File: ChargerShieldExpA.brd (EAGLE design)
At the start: 160 x 99.1 mm, 101 parts, among them IC1 TL431, IC2 LM324N, Q1 BUZ11, Q2 BD648, Q3 BUZ171, Q4 IRFZ48Z, T1 BC548, X1 +Vin, X2 VCC, X3 Battery

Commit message: update
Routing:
- net GND: track 168.7 -> 169.3 mm
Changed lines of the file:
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@@
 <setting verticaltext="up"/>
 </settings>
-<grid distance="1.27" unitdist="mm" unit="mm" style="lines" multiple="2" display="yes" altdistance="0.15875" altunitdist="mm" altunit="mm"/>
+<grid distance="0.05" unitdist="inch" unit="mm" style="lines" multiple="1" display="yes" altdistance="0.025" altunitdist="inch" altunit="mm"/>
 <layers>
 <layer number="1" name="Top" color="4" fill="1" visible="yes" active="yes"/>
@@
 <wire x1="19.05" y1="11.43" x2="19.05" y2="-3.81" width="0.8128" layer="1" style="shortdash"/>
 <contactref element="JP20" pad="3"/>
-<via x="5.08" y="38.1" extent="1-16" drill="0.8" shape="square"/>
+<via x="5.08" y="38.1" extent="1-16" drill="1" shape="square"/>
 <wire x1="22.86" y1="-7.62" x2="22.86" y2="-11.47" width="1.6764" layer="16"/>
 <wire x1="22.86" y1="-11.47" x2="22.82" y2="-10.16" width="1.6764" layer="16"/>
@@
 <contactref element="S4" pad="1"/>
 <contactref element="S5" pad="1"/>
-<via x="1.27" y="38.1" extent="1-16" drill="0.8" shape="square"/>
-<wire x1="1.27" y1="38.1" x2="5.08" y2="38.1" width="0.8128" layer="1"/>
+<via x="0.635" y="38.1" extent="1-16" drill="1" shape="square"/>
+<wire x1="0.635" y1="38.1" x2="5.08" y2="38.1" width="0.8128" layer="1"/>
 <wire x1="2.54" y1="33.02" x2="2.54" y2="12.7" width="2.54" layer="16"/>
 <wire x1="2.54" y1="33.02" x2="6.35" y2="33.02" width="2.54" layer="16"/>
@@
 <polygon width="1.27" layer="16" isolate="0.6096" orphans="yes">
 <vertex x="0" y="-15.24"/>
-<vertex x="1.27" y="53.34"/>
+<vertex x="0" y="35.56"/>
+<vertex x="-12.7" y="35.56"/>
+<vertex x="-12.7" y="53.34"/>
 <vertex x="-41.91" y="53.34"/>
 <vertex x="-43.18" y="-15.24"/>
@@
 <wire x1="-27.94" y1="59.69" x2="-27.94" y2="58.42" width="0.8128" layer="16"/>
 <wire x1="-27.94" y1="58.42" x2="-11.43" y2="41.91" width="0.8128" layer="16"/>
-<wire x1="-11.43" y1="41.91" x2="-11.43" y2="29.21" width="0.8128" layer="16"/>
+<wire x1="-11.43" y1="41.91" x2="-11.43" y2="27.94" width="0.8128" layer="16"/>
 <wire x1="-40.64" y1="17.78" x2="-40.64" y2="8.1788" width="0.8128" layer="16"/>
 <wire x1="-40.64" y1="8.1788" x2="-38.735" y2="6.2738" width="0.8128" layer="16"/>
-<wire x1="-11.43" y1="29.21" x2="-16.51" y2="24.13" width="0.8128" layer="16"/>
-<wire x1="-16.51" y1="24.13" x2="-16.51" y2="17.78" width="0.8128" layer="16"/>
+<wire x1="-11.43" y1="27.94" x2="-16.51" y2="22.86" width="0.8128" layer="16"/>
+<wire x1="-16.51" y1="22.86" x2="-16.51" y2="17.78" width="0.8128" layer="16"/>
 <wire x1="-16.51" y1="17.78" x2="-40.64" y2="17.78" width="0.8128" layer="16"/>
 <contactref element="U$3" pad="6"/>

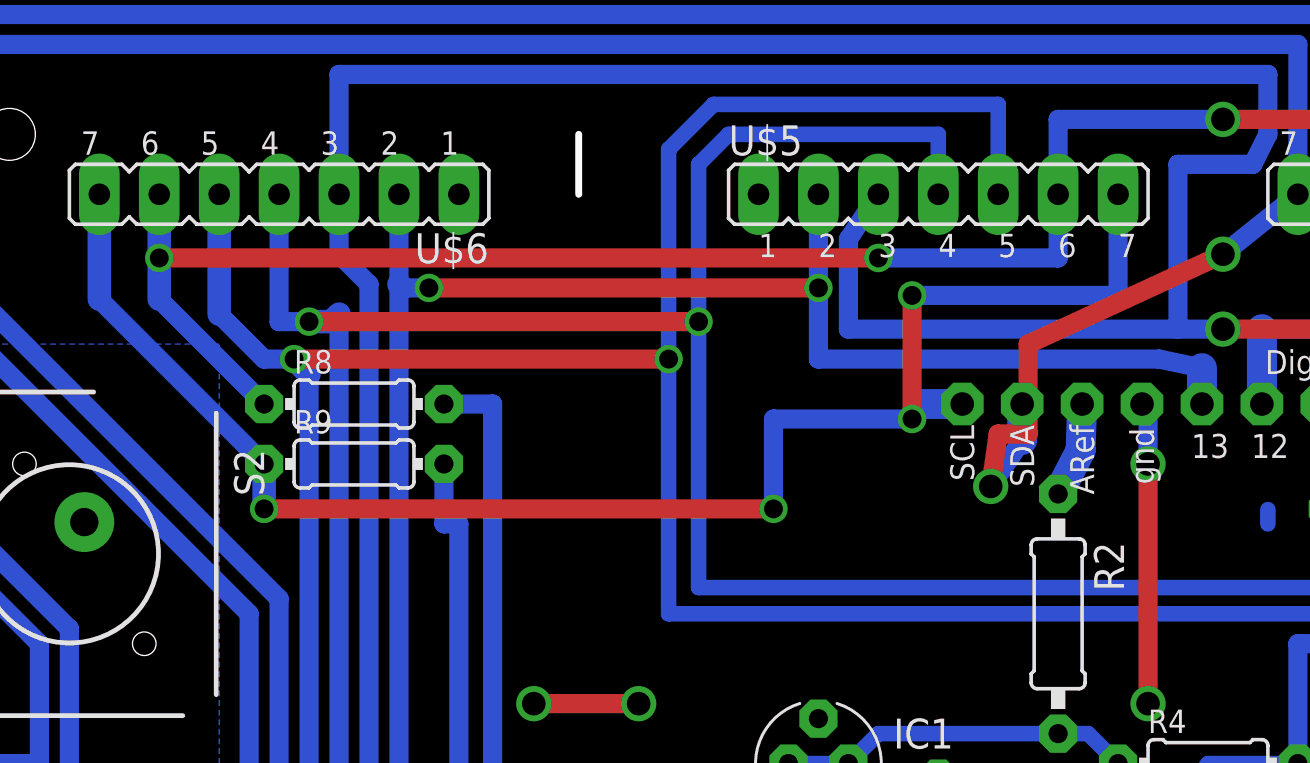
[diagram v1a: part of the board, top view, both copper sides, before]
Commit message: via drills should be 1mm
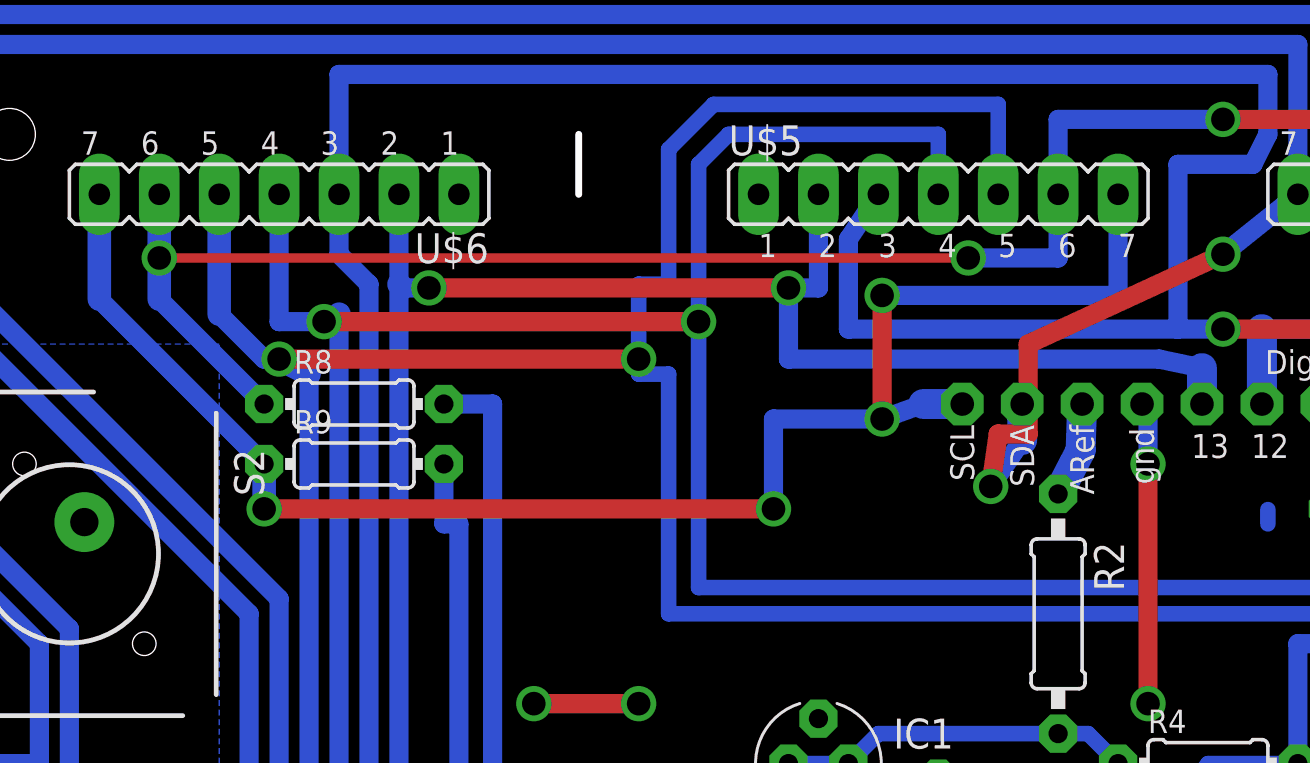
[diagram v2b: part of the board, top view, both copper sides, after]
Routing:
- net PWM_DISCHARGE2: track 188.2 -> 190.0 mm
- net N$1: track 101.7 -> 103.0 mm
- net N$41: track 68.2 -> 69.3 mm
- net PWM_DISCHARGE1: track 170.6 -> 170.0 mm
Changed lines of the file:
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@@
 <wire x1="28.956" y1="50.8" x2="28.956" y2="52.324" width="1.27" layer="16"/>
 <wire x1="28.956" y1="52.324" x2="27.14625" y2="52.705" width="0.8128" layer="16"/>
-<wire x1="27.14625" y1="52.705" x2="12.7" y2="52.705" width="0.8128" layer="16"/>
-<wire x1="12.7" y1="52.705" x2="12.7" y2="55.72125" width="0.8128" layer="16"/>
+<wire x1="27.14625" y1="52.705" x2="11.43" y2="52.705" width="0.8128" layer="16"/>
+<wire x1="11.43" y1="52.705" x2="11.43" y2="55.72125" width="0.8128" layer="16"/>
 <contactref element="R3" pad="2"/>
 <contactref element="U$6" pad="2"/>
+<wire x1="11.43" y1="55.72125" x2="12.7" y2="55.72125" width="0.8128" layer="16"/>
 <wire x1="12.7" y1="55.72125" x2="12.7" y2="59.69" width="0.8128" layer="16"/>
 <wire x1="-4.445" y1="1.27" x2="-4.445" y2="2.54" width="0.8128" layer="16"/>
@@
 <wire x1="-3.81" y1="55.72125" x2="-4.92125" y2="55.72125" width="0.8128" layer="16"/>
 <wire x1="-5.08" y1="55.88" x2="-5.08" y2="59.69" width="0.8128" layer="16"/>
-<wire x1="-3.81" y1="55.72125" x2="12.7" y2="55.72125" width="0.8128" layer="1"/>
-<via x="12.7" y="55.72125" extent="1-16" drill="0.8" shape="square"/>
-<via x="-3.81" y="55.72125" extent="1-16" drill="0.8" shape="square"/>
+<wire x1="-3.81" y1="55.72125" x2="11.43" y2="55.72125" width="0.8128" layer="1"/>
+<via x="11.43" y="55.72125" extent="1-16" drill="1" shape="square"/>
+<via x="-3.81" y="55.72125" extent="1-16" drill="1" shape="square"/>
 </signal>
 <signal name="N$2">
@@
 <contactref element="U$6" pad="4"/>
 <wire x1="-10.16" y1="59.69" x2="-10.16" y2="54.2925" width="0.8128" layer="16"/>
-<wire x1="-10.16" y1="54.2925" x2="-8.89" y2="54.2925" width="0.8128" layer="16"/>
-<wire x1="-8.89" y1="54.2925" x2="-7.9375" y2="54.2925" width="1" layer="16"/>
+<wire x1="-10.16" y1="54.2925" x2="-8.255" y2="54.2925" width="0.8128" layer="16"/>
+<wire x1="-8.255" y1="54.2925" x2="-7.9375" y2="54.2925" width="1" layer="16"/>
 <wire x1="-7.9375" y1="54.2925" x2="-7.62" y2="54.61" width="1" layer="16"/>
 <wire x1="-7.62" y1="54.61" x2="-7.62" y2="-2.54" width="0.8128" layer="16"/>
@@
 <wire x1="-19.05" y1="-2.54" x2="-19.05" y2="-10.16" width="0.8128" layer="16"/>
 <wire x1="-19.05" y1="-10.16" x2="-16.51" y2="-10.16" width="0.8128" layer="16"/>
-<via x="-8.89" y="54.2925" extent="1-16" drill="0.8" shape="square"/>
-<wire x1="-8.89" y1="54.2925" x2="7.62" y2="54.2925" width="0.8128" layer="1"/>
-<via x="7.62" y="54.2925" extent="1-16" drill="0.8" shape="square"/>
+<via x="-8.255" y="54.2925" extent="1-16" drill="1" shape="square"/>
+<wire x1="-8.255" y1="54.2925" x2="7.62" y2="54.2925" width="0.8128" layer="1"/>
+<via x="7.62" y="54.2925" extent="1-16" drill="1" shape="square"/>
 </signal>
 <signal name="PWM_CHARGE1">
@@
 <wire x1="8.255" y1="63.5" x2="20.32" y2="63.5" width="0.6604" layer="16"/>
 <wire x1="6.35" y1="61.595" x2="8.255" y2="63.5" width="0.6604" layer="16"/>
-<wire x1="6.35" y1="41.91" x2="6.35" y2="52.705" width="0.6604" layer="16"/>
-<wire x1="6.35" y1="52.705" x2="6.35" y2="61.595" width="0.6604" layer="16"/>
+<wire x1="6.35" y1="41.91" x2="6.35" y2="52.07" width="0.6604" layer="16"/>
+<wire x1="6.35" y1="52.07" x2="5.08" y2="52.07" width="0.6604" layer="16"/>
+<wire x1="5.08" y1="52.07" x2="5.08" y2="52.705" width="0.6604" layer="16"/>
+<wire x1="5.08" y1="52.705" x2="5.08" y2="55.88" width="0.6604" layer="16"/>
+<wire x1="5.08" y1="55.88" x2="6.35" y2="55.88" width="0.6604" layer="16"/>
+<wire x1="6.35" y1="55.88" x2="6.35" y2="61.595" width="0.6604" layer="16"/>
 <wire x1="36.83" y1="41.91" x2="6.35" y2="41.91" width="0.6604" layer="16"/>
 <wire x1="39.21125" y1="44.45" x2="36.83" y2="41.91" width="0.6604" layer="16"/>
@@
 <wire x1="-12.7" y1="59.69" x2="-12.7" y2="54.61" width="1" layer="16"/>
 <wire x1="-12.7" y1="54.61" x2="-10.795" y2="52.705" width="0.8128" layer="16"/>
-<wire x1="-10.795" y1="52.705" x2="-9.525" y2="52.705" width="0.8128" layer="16"/>
-<wire x1="-9.525" y1="52.705" x2="-8.89" y2="52.07" width="1" layer="16"/>
+<wire x1="-10.795" y1="52.705" x2="-10.16" y2="52.705" width="0.8128" layer="16"/>
+<wire x1="-10.16" y1="52.705" x2="-8.89" y2="52.07" width="1" layer="16"/>
 <wire x1="-8.89" y1="52.07" x2="-8.89" y2="-1.27" width="0.8128" layer="16"/>
 <wire x1="-8.89" y1="-1.27" x2="-21.59" y2="-1.27" width="0.8128" layer="16"/>
 <wire x1="-21.59" y1="-1.27" x2="-21.59" y2="-13.97" width="0.8128" layer="16"/>
 <wire x1="-21.59" y1="-13.97" x2="-16.51" y2="-13.97" width="0.8128" layer="16"/>
-<via x="-9.525" y="52.705" extent="1-16" drill="0.8" shape="square"/>
-<wire x1="-9.525" y1="52.705" x2="6.35" y2="52.705" width="0.8128" layer="1"/>
-<via x="6.35" y="52.705" extent="1-16" drill="0.8" shape="square"/>
+<via x="-10.16" y="52.705" extent="1-16" drill="1" shape="square"/>
+<wire x1="-10.16" y1="52.705" x2="5.08" y2="52.705" width="0.8128" layer="1"/>
+<via x="5.08" y="52.705" extent="1-16" drill="1" shape="square"/>
 </signal>
 <signal name="N$24">
@@
 <wire x1="-17.78" y1="55.245" x2="-17.78" y2="59.69" width="1" layer="16"/>
 <wire x1="-10.795" y1="48.26" x2="-10.795" y2="46.355" width="1" layer="16"/>
-<via x="-10.795" y="46.355" extent="1-16" drill="0.8" shape="square"/>
+<via x="-10.795" y="46.355" extent="1-16" drill="1" shape="square"/>
 <wire x1="-10.795" y1="46.355" x2="10.795" y2="46.355" width="0.8128" layer="1"/>
-<via x="10.795" y="46.355" extent="1-16" drill="0.8" shape="square"/>
+<via x="10.795" y="46.355" extent="1-16" drill="1" shape="square"/>
 <wire x1="10.795" y1="46.355" x2="10.795" y2="50.165" width="0.8128" layer="16"/>
-<wire x1="10.795" y1="50.165" x2="16.66875" y2="50.165" width="0.8128" layer="16"/>
-<via x="16.66875" y="50.165" extent="1-16" drill="0.8" shape="square"/>
-<wire x1="16.66875" y1="50.165" x2="16.66875" y2="55.40375" width="0.8128" layer="1"/>
-<via x="16.66875" y="55.40375" extent="1-16" drill="0.8" shape="square"/>
-<wire x1="16.66875" y1="55.40375" x2="25.4" y2="55.40375" width="0.8128" layer="16"/>
+<wire x1="10.795" y1="50.165" x2="15.39875" y2="50.165" width="0.8128" layer="16"/>
+<via x="15.39875" y="50.165" extent="1-16" drill="1" shape="square"/>
+<wire x1="15.39875" y1="50.165" x2="15.39875" y2="55.40375" width="0.8128" layer="1"/>
+<via x="15.39875" y="55.40375" extent="1-16" drill="1" shape="square"/>
+<wire x1="15.39875" y1="55.40375" x2="25.4" y2="55.40375" width="0.8128" layer="16"/>
 <wire x1="25.4" y1="55.40375" x2="25.4" y2="59.69" width="0.8128" layer="16"/>
 <wire x1="18.796" y1="50.8" x2="17.145" y2="50.8" width="1.27" layer="16"/>
-<wire x1="17.145" y1="50.8" x2="16.66875" y2="50.165" width="0.8128" layer="16"/>
+<wire x1="17.145" y1="50.8" x2="15.39875" y2="50.165" width="0.8128" layer="16"/>
 </signal>
 <signal name="N$4">
@@
 <wire x1="-15.24" y1="56.99125" x2="-15.24" y2="59.69" width="1" layer="16"/>
 <wire x1="22.86" y1="59.69" x2="22.86" y2="56.99125" width="0.8128" layer="16"/>
-<wire x1="22.86" y1="56.99125" x2="15.24" y2="56.99125" width="0.8128" layer="16"/>
-<via x="15.24" y="56.99125" extent="1-16" drill="0.8" shape="square"/>
-<wire x1="15.24" y1="56.99125" x2="-15.24" y2="56.99125" width="0.8128" layer="1"/>
-<via x="-15.24" y="56.99125" extent="1-16" drill="0.8" shape="square"/>
+<wire x1="22.86" y1="56.99125" x2="19.05" y2="56.99125" width="0.8128" layer="16"/>
+<via x="19.05" y="56.99125" extent="1-16" drill="1" shape="square"/>
+<wire x1="19.05" y1="56.99125" x2="-15.24" y2="56.99125" width="0.4026" layer="1"/>
+<via x="-15.24" y="56.99125" extent="1-16" drill="1" shape="square"/>
 <wire x1="22.86" y1="59.69" x2="22.86" y2="62.865" width="0.8128" layer="16"/>
 <wire x1="22.86" y1="62.865" x2="29.845" y2="62.865" width="0.8128" layer="16"/>
